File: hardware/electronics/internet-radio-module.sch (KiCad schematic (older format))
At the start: 2 parts

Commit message: Main wiring diagram
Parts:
- added J1: JACK_TRS_6PINS, symbol JACK_TRS_6PINS
- added RV1: POT_TRIM, symbol POT_TRIM
- added SW2: SW_SPST, symbol SW_SPST
- gave numbers to parts that had none: 2
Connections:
- net VDD is gone; now on net +5V: DS1.2 (VDD)
- net VSS is gone; now on net GND: DS1.1 (VSS)
- net AUDIO-LEFT: now also J1.2 (T)
- net AUDIO-RIGHT: now also J1.3 (R)
- net GND: now also DS1.16 (LED-), DS1.5 (R/W), J1.1 (S), RV1.3
- net +5V: now reaches DS1.15 (LED+)
- net +5V: now also RV1.1
- net at DS1.3 (VO): now also RV1.2
- net RS: now reaches DS1.4 (RS)
- net EN: now reaches DS1.6 (E)
- net D0: no longer names the net of DS1.7 (D0)
- net D1: no longer names the net of DS1.8 (D1)
- net D2: no longer names the net of DS1.9 (D2)
- net D3: no longer names the net of DS1.10 (D3)
- new net +12V: SW2.1 (A), SW2.2 (B)
- no-connect marks 0 -> 4
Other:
- note added: "EXTERNAL SUPPLY"
- note added: "POWER \nSWITCH"
- moved on the sheet: DS1

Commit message: Contrast pot on PCB; Control button symbol changed
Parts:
- removed RV1: POT_TRIM, symbol POT_TRIM
- removed SW1: SW_PUSH_SMALL, symbol SW_PUSH_SMALL
- added SW1: SW_Push, symbol SW_Push
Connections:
- net CONTROL: now also SW1.2
- net GND: now also SW1.1
- net CONTRAST: now reaches DS1.3 (VO)
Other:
- note added: "CONTROL\nBUTTON"
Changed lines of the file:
@@
 AUDIO-RIGHT
-$Comp
-L SW_PUSH_SMALL SW1
-U 1 1 5D30B510
-P 2300 3850
-F 0 "SW1" H 2300 3750 60  0000 C CNN
-F 1 "SW_PUSH_SMALL" H 2300 4100 60  0000 C CNN
-F 2 "" H 2480 3850 60  0001 C CNN
-F 3 "" H 2480 3850 60  0001 C CNN
-	1    2300 3850
-	1    0    0    -1
-$EndComp
 $Comp
 L GND #PWR10
 U 1 1 5D30B533
-P 2050 4250
-F 0 "#PWR10" H 2050 4000 50  0001 C CNN
-F 1 "GND" H 2050 4100 50  0000 C CNN
-F 2 "" H 2050 4250 50  0000 C CNN
-F 3 "" H 2050 4250 50  0000 C CNN
-	1    2050 4250
-	1    0    0    -1
-$EndComp
-Wire Wire Line
-	2050 3800 2050 4250
+P 2100 4250
+F 0 "#PWR10" H 2100 4000 50  0001 C CNN
+F 1 "GND" H 2100 4100 50  0000 C CNN
+F 2 "" H 2100 4250 50  0000 C CNN
+F 3 "" H 2100 4250 50  0000 C CNN
+	1    2100 4250
+	1    0    0    -1
+$EndComp
+Wire Wire Line
+	2100 3800 2100 4250
 Text HLabel 3550 3800 2    60   Input ~ 0
 CONTROL
@@
 $EndComp
 Wire Wire Line
-	2550 3800 3550 3800
-Wire Wire Line
-	2550 3900 2550 3800
+	2500 3800 3550 3800
 Text HLabel 5500 5150 1    60   Output ~ 0
 GND
@@
 Wire Wire Line
 	6300 1850 6300 2700
-$Comp
-L POT_TRIM RV1
-U 1 1 5D31BED5
-P 4500 2250
-F 0 "RV1" V 4325 2250 50  0000 C CNN
-F 1 "POT_TRIM" V 4400 2250 50  0000 C CNN
-F 2 "" H 4500 2250 50  0000 C CNN
-F 3 "" H 4500 2250 50  0000 C CNN
-	1    4500 2250
-	1    0    0    -1
-$EndComp
-Wire Wire Line
-	4650 2250 4700 2250
-Wire Wire Line
-	4700 2250 4700 2350
+Wire Wire Line
+	4700 2650 4700 2350
+Wire Wire Line
+	4700 2350 4700 2350
 Wire Wire Line
 	4700 2350 5200 2350
 Wire Wire Line
 	5200 2350 5200 1850
-Wire Wire Line
-	4500 2100 4500 1950
-Wire Wire Line
-	4500 2400 4500 2500
-$Comp
-L GND #PWR7
-U 1 1 5D31BF74
-P 4500 2500
-F 0 "#PWR7" H 4500 2250 50  0001 C CNN
-F 1 "GND" H 4500 2350 50  0000 C CNN
-F 2 "" H 4500 2500 50  0000 C CNN
-F 3 "" H 4500 2500 50  0000 C CNN
-	1    4500 2500
-	1    0    0    -1
-$EndComp
 Wire Wire Line
 	5500 5150 5500 6100
@@
 Wire Wire Line
 	5100 1850 5100 2050
-$Comp
-L +5V #PWR4
-U 1 1 5D31C6F5
-P 4500 1950
-F 0 "#PWR4" H 4500 1800 50  0001 C CNN
-F 1 "+5V" H 4500 2090 50  0000 C CNN
-F 2 "" H 4500 1950 50  0000 C CNN
-F 3 "" H 4500 1950 50  0000 C CNN
-	1    4500 1950
-	1    0    0    -1
-$EndComp
 $Comp
 L GND #PWR3
@@
 Text Notes 4800 6400 0    60   ~ 0
 EXTERNAL SUPPLY
+$Comp
+L SW_Push SW1
+U 1 1 5D31EEDC
+P 2300 3800
+F 0 "SW1" H 2350 3900 50  0000 L CNN
+F 1 "SW_Push" H 2300 3740 50  0000 C CNN
+F 2 "" H 2300 4000 50  0001 C CNN
+F 3 "" H 2300 4000 50  0001 C CNN
+	1    2300 3800
+	1    0    0    -1
+$EndComp
+Wire Notes Line
+	2000 3500 2000 4100
+Wire Notes Line
+	2000 4100 2900 4100
+Wire Notes Line
+	2900 4100 2900 3500
+Wire Notes Line
+	2900 3500 2000 3500
+Text Notes 2500 4100 0    60   ~ 0
+CONTROL\nBUTTON
+Text HLabel 4700 2650 3    60   Input ~ 0
+CONTRAST
 $EndSCHEMATC

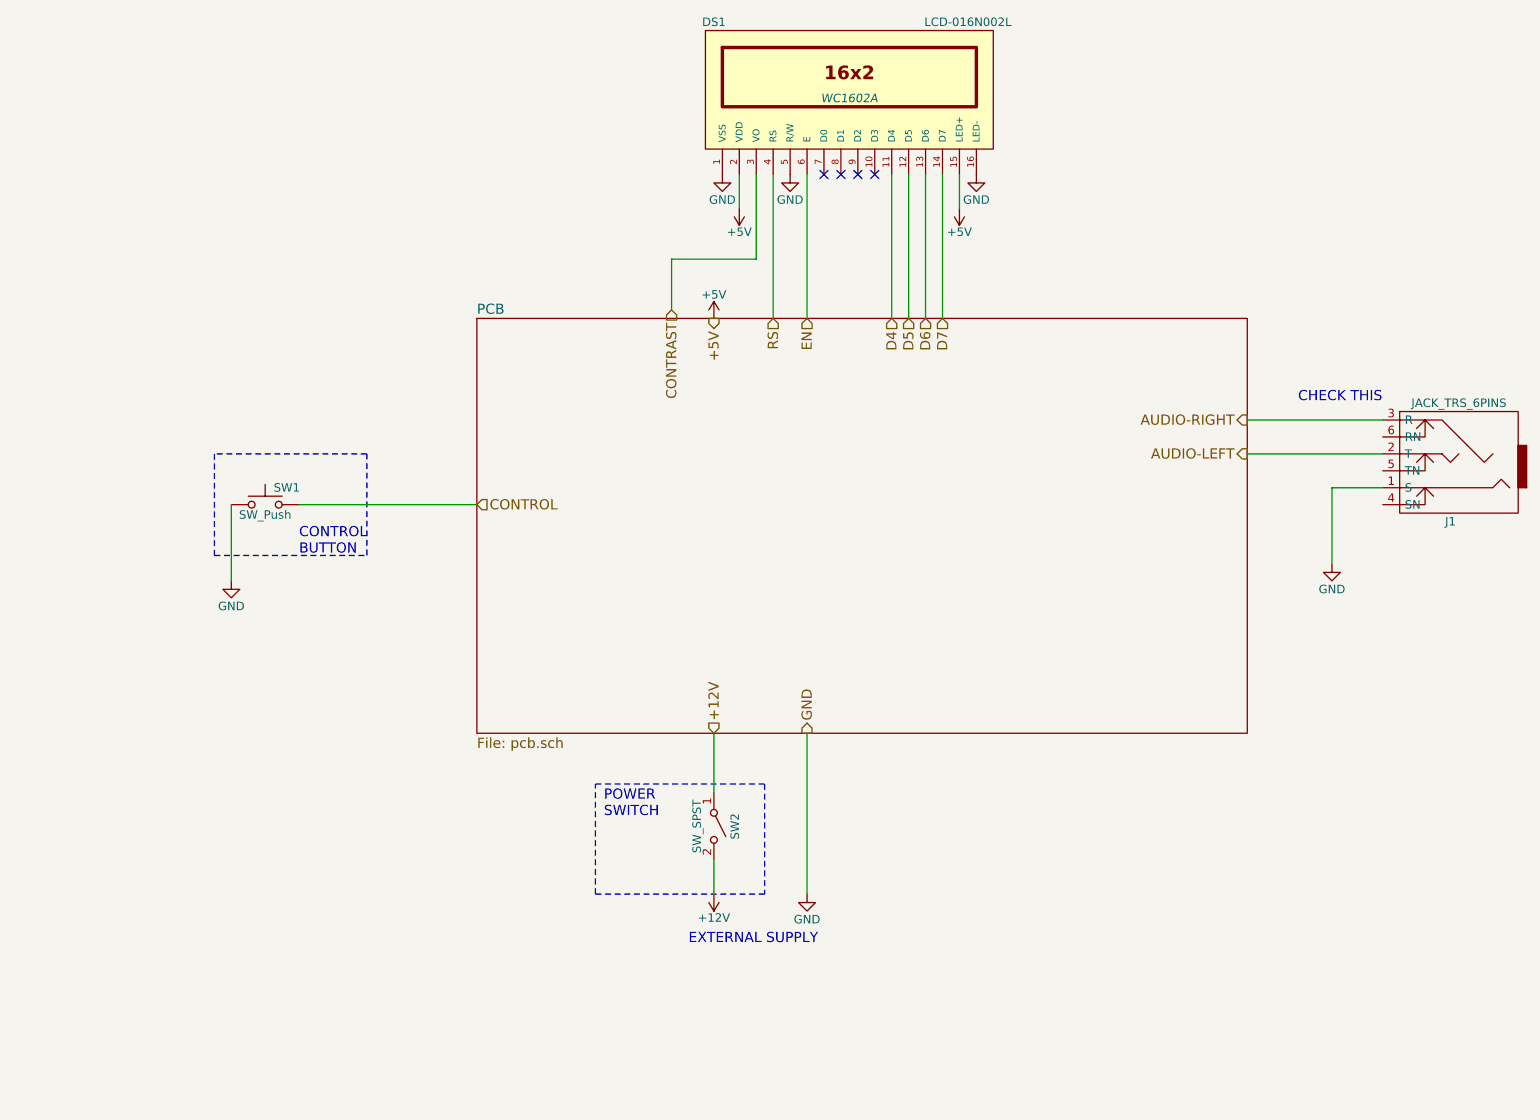
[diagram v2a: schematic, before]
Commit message: Breadboard components added
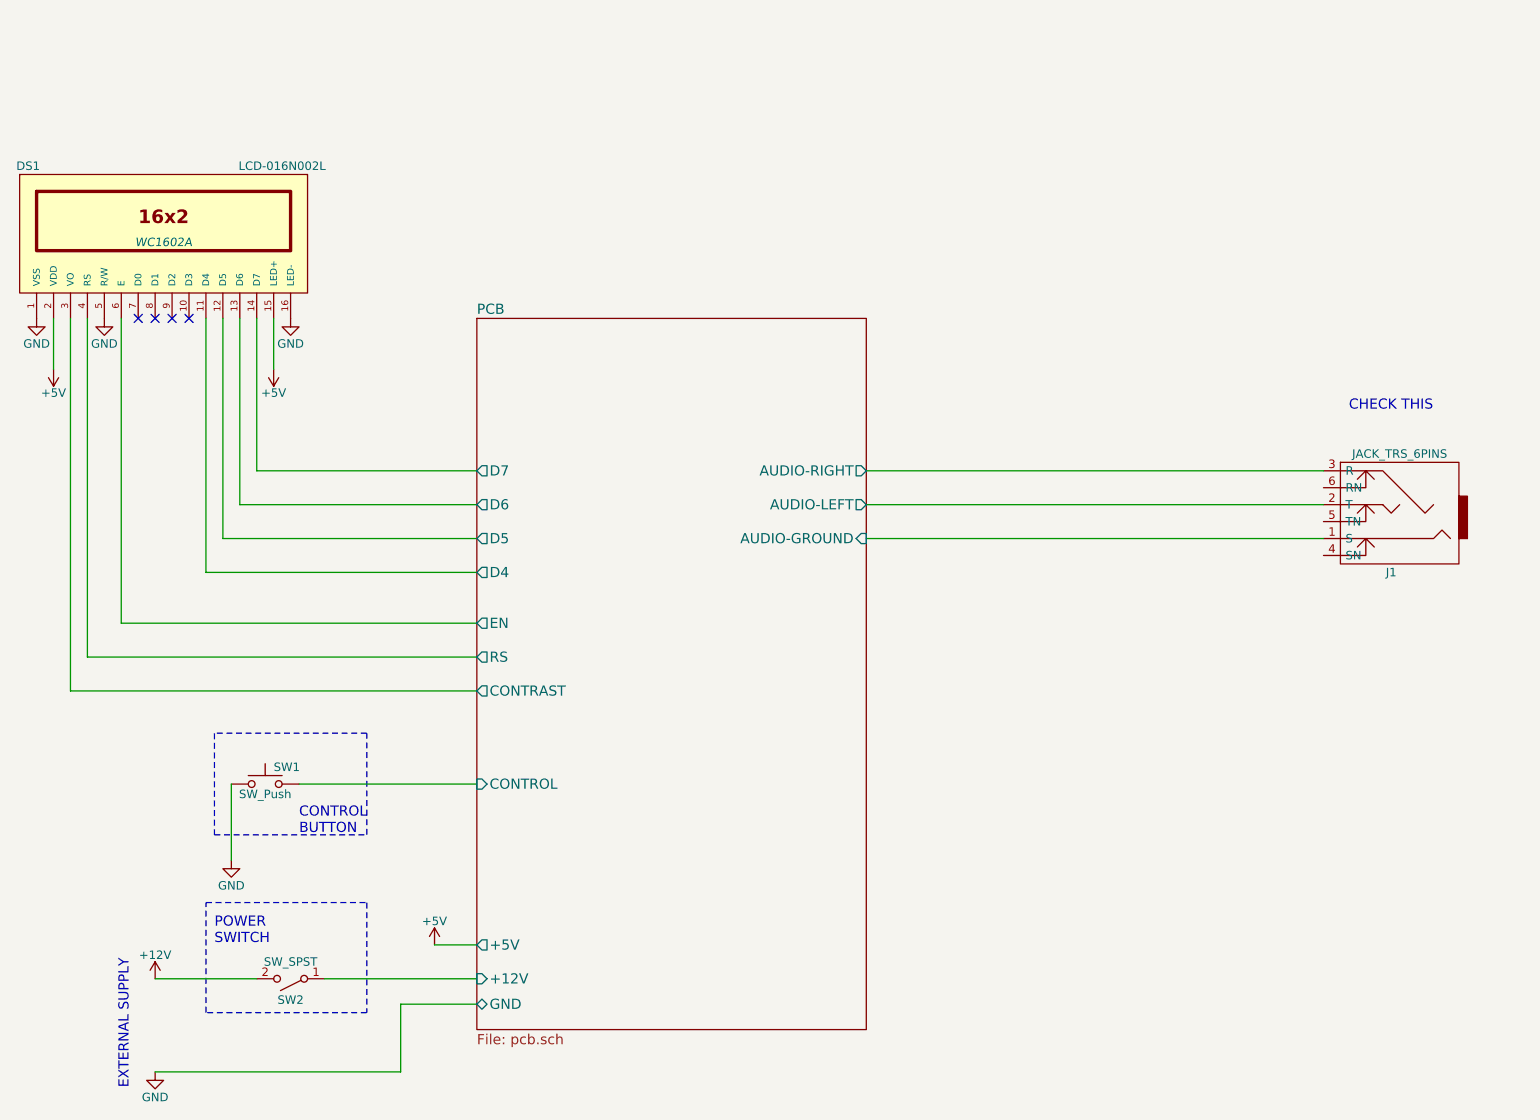
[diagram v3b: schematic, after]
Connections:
- net +12V: no longer SW2.1 (A)
- net GND: no longer J1.1 (S)
- net AUDIO-LEFT renamed PCB/AUDIO-LEFT
- net AUDIO-RIGHT renamed PCB/AUDIO-RIGHT
- net CONTRAST renamed PCB/CONTRAST
- net CONTROL renamed PCB/CONTROL
- net D4 renamed PCB/D4
- net D5 renamed PCB/D5
- net D6 renamed PCB/D6
- net D7 renamed PCB/D7
- net EN renamed PCB/EN
- net RS renamed PCB/RS
- new net PCB/+12V: SW2.1 (A)
- new net PCB/AUDIO-GROUND: J1.1 (S)
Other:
- moved on the sheet: DS1, J1, SW1, SW2

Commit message: Added level shifting buffers
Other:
- note added: "1"
- note added: "16"
- note added: "Pin Layout LCD / Top View"
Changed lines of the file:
@@
 LIBS:Switch
 LIBS:SparkFun-Boards
-LIBS:adafruit
 LIBS:internet-radio-module-cache
 EELAYER 25 0
@@
 Wire Notes Line
 	1950 6800 1950 6150
+Text Notes 1050 1150 0    60   ~ 0
+1
+Text Notes 1800 1150 0    60   ~ 0
+16
+Wire Notes Line
+	1000 1050 2300 1050
+Wire Notes Line
+	1000 1050 1000 1400
+Wire Notes Line
+	1000 1400 2300 1400
+Wire Notes Line
+	2300 1400 2300 1050
+Wire Notes Line
+	1150 1200 1150 1350
+Wire Notes Line
+	1150 1350 2150 1350
+Wire Notes Line
+	2150 1350 2150 1200
+Wire Notes Line
+	2150 1200 1150 1200
+Text Notes 1050 1500 0    60   ~ 0
+Pin Layout LCD / Top View
 $EndSCHEMATC
